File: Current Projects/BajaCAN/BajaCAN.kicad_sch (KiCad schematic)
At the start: 36 parts, among them J1 348300801, J2 348302001, J3 348302004, J4 348300804, SW1 MVIO, U1 MCP1603, U2 MCP251863T-H-SS, U3 AVR128DB32x-xPT, Y1 OV-7604-C7, Y2 CSTNE20M0V530000R0

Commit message: Linked most footprints for Node board
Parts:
- C1, C10, C11, C2, C3, C4, C5, C6, C8, C9: footprint (none) -> Capacitor_SMD:C_0603_1608Metric
- C7: footprint (none) -> Capacitor_SMD:C_Elec_4x5.4
- D1: footprint (none) -> LED_SMD:LED_0805_2012Metric
- L1: footprint (none) -> Inductor_SMD:L_1008_2520Metric
- R1, R2: footprint (none) -> Resistor_SMD:R_0603_1608Metric
- TP1, TP2, TP4: footprint (none) -> TestPoint:TestPoint_Pad_D2.0mm
- TP10, TP5, TP6, TP7, TP8, TP9: footprint (none) -> TestPoint:TestPoint_Pad_D1.0mm
- TP3: footprint (none) -> TestPoint:TestPoint_Pad_D1.5mm
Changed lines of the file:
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@@
 			)
 		)
-		(property "Footprint" ""
+		(property "Footprint" "Capacitor_SMD:C_0603_1608Metric"
 			(at 130.81 41.91 0)
 			(effects
@@
 			)
 		)
-		(property "Footprint" ""
+		(property "Footprint" "TestPoint:TestPoint_Pad_D1.0mm"
 			(at 105.41 71.12 0)
 			(effects
@@
 			)
 		)
-		(property "Footprint" ""
+		(property "Footprint" "TestPoint:TestPoint_Pad_D1.0mm"
 			(at 107.95 73.66 0)
 			(effects
@@
 			)
 		)
-		(property "Footprint" ""
+		(property "Footprint" "TestPoint:TestPoint_Pad_D1.5mm"
 			(at 95.25 49.53 0)
 			(effects
@@
 			)
 		)
-		(property "Footprint" ""
+		(property "Footprint" "Capacitor_SMD:C_0603_1608Metric"
 			(at 146.05 41.91 0)
 			(effects
@@
 			)
 		)
-		(property "Footprint" ""
+		(property "Footprint" "Capacitor_SMD:C_0603_1608Metric"
 			(at 68.58 38.1 0)
 			(effects
@@
 			)
 		)
-		(property "Footprint" ""
+		(property "Footprint" "TestPoint:TestPoint_Pad_D1.0mm"
 			(at 163.83 54.61 0)
 			(effects
@@
 			)
 		)
-		(property "Footprint" ""
+		(property "Footprint" "TestPoint:TestPoint_Pad_D2.0mm"
 			(at 175.26 41.91 0)
 			(effects
@@
 			)
 		)
-		(property "Footprint" ""
+		(property "Footprint" "TestPoint:TestPoint_Pad_D1.0mm"
 			(at 109.22 58.42 0)
 			(effects
@@
 			)
 		)
-		(property "Footprint" ""
+		(property "Footprint" "Capacitor_SMD:C_0603_1608Metric"
 			(at 68.58 41.91 0)
 			(effects
@@
 			)
 		)
-		(property "Footprint" ""
+		(property "Footprint" "Inductor_SMD:L_1008_2520Metric"
 			(at 102.87 22.86 0)
 			(effects
@@
 			)
 		)
-		(property "Footprint" ""
+		(property "Footprint" "Capacitor_SMD:C_Elec_4x5.4"
 			(at 171.45 43.18 0)
 			(effects
@@
 			)
 		)
-		(property "Footprint" ""
+		(property "Footprint" "Capacitor_SMD:C_0603_1608Metric"
 			(at 82.55 49.53 0)
 			(effects
@@
 			)
 		)
-		(property "Footprint" ""
+		(property "Footprint" "Capacitor_SMD:C_0603_1608Metric"
 			(at 105.41 29.21 0)
 			(effects
@@
 			)
 		)
-		(property "Footprint" ""
+		(property "Footprint" "TestPoint:TestPoint_Pad_D2.0mm"
 			(at 107.95 22.86 0)
 			(effects
@@
 			)
 		)
-		(property "Footprint" ""
+		(property "Footprint" "TestPoint:TestPoint_Pad_D2.0mm"
 			(at 175.26 46.99 0)
 			(effects
@@
 			)
 		)
-		(property "Footprint" ""
+		(property "Footprint" "Capacitor_SMD:C_0603_1608Metric"
 			(at 62.23 138.43 0)
 			(effects
@@
 			)
 		)
-		(property "Footprint" ""
+		(property "Footprint" "TestPoint:TestPoint_Pad_D1.0mm"
 			(at 153.67 62.23 0)
 			(effects
@@
 			)
 		)
-		(property "Footprint" ""
+		(property "Footprint" "Resistor_SMD:R_0603_1608Metric"
 			(at 158.75 58.42 0)
 			(effects
@@
 			)
 		)
-		(property "Footprint" ""
+		(property "Footprint" "LED_SMD:LED_0805_2012Metric"
 			(at 33.02 24.13 0)
 			(effects
@@
 			)
 		)
-		(property "Footprint" ""
+		(property "Footprint" "Capacitor_SMD:C_0603_1608Metric"
 			(at 30.48 49.53 0)
 			(effects
@@
 			)
 		)
-		(property "Footprint" ""
+		(property "Footprint" "TestPoint:TestPoint_Pad_D1.0mm"
 			(at 111.76 60.96 0)
 			(effects
@@
 			)
 		)
-		(property "Footprint" ""
+		(property "Footprint" "Capacitor_SMD:C_0603_1608Metric"
 			(at 130.81 45.72 0)
 			(effects
@@
 			)
 		)
-		(property "Footprint" ""
+		(property "Footprint" "Resistor_SMD:R_0603_1608Metric"
 			(at 41.91 25.908 90)
 			(effects
@@
 			)
 		)
-		(property "Footprint" ""
+		(property "Footprint" "Capacitor_SMD:C_0603_1608Metric"
 			(at 78.74 26.67 0)
 			(effects

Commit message: Revert "Merge branch 'main' of github.com:wmBaja/PCB-Design"
This reverts commit fce7a7b580b52db6ba8267641ace841e509f0b35, reversing
changes made to 0a8d1a67a362b0eb6635e51fbc998032cda9d21d.
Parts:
- removed C10: 0.1u, Capacitor_SMD:C_0603_1608Metric, symbol Device:C_Small
- removed D1: POWER, LED_SMD:LED_0805_2012Metric, symbol Device:LED
- removed J1: 348300801, molex:CONN_SD-34829-001_08_ST_MOL, symbol molex:348300801
- removed J4: 348300804, molex:CONN_SD-34829-001_08_ST_MOL, symbol molex:348300801
- removed R1: 1k, Resistor_SMD:R_0603_1608Metric, symbol Device:R
- removed SW1: MVIO, symbol Switch:SW_SPDT
- removed TP1, TP2, TP4: TestPoint, TestPoint:TestPoint_Pad_D2.0mm, symbol Connector:TestPoint
- removed TP10, TP5, TP6, TP7, TP8, TP9: TestPoint, TestPoint:TestPoint_Pad_D1.0mm, symbol Connector:TestPoint
- removed TP3: TestPoint, TestPoint:TestPoint_Pad_D1.5mm, symbol Connector:TestPoint
- added J1: Conn_01x04, symbol Connector_Generic:Conn_01x04
- added J2: ICSP, symbol Connector_Generic:Conn_02x03_Odd_Even
- C1: renamed from C9; footprint Capacitor_SMD:C_0603_1608Metric -> (none)
- C10: renamed from C7; value 10u -> 0.1u; footprint Capacitor_SMD:C_Elec_4x5.4 -> (none)
- C2: renamed from C11; footprint Capacitor_SMD:C_0603_1608Metric -> (none)
- C3, C4, C5: footprint Capacitor_SMD:C_0603_1608Metric -> (none)
- C6: renamed from C8; footprint Capacitor_SMD:C_0603_1608Metric -> (none)
- C7: renamed from C6; footprint Capacitor_SMD:C_0603_1608Metric -> (none)
- C8: renamed from C1; footprint Capacitor_SMD:C_0603_1608Metric -> (none)
- C9: renamed from C2; footprint Capacitor_SMD:C_0603_1608Metric -> (none)
- L1: footprint Inductor_SMD:L_1008_2520Metric -> (none)
- R2: footprint Resistor_SMD:R_0603_1608Metric -> (none)
- Y2: value CSTNE20M0V530000R0 -> CSTNE16M0VH3C000R0
- renumbered D2 to D1, J2 to J3, J3 to J4, U3 to U1, U1 to U3, U2 to U4
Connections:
- net +3.3V: now also U1.10 (VDDIO2)
- net +5V: now also C2.1, J1.1 (Pin_1), J2.2 (Pin_2); no longer C2.2
- net CAN_H: now also J1.3 (Pin_3)
- net CAN_L: now also J1.4 (Pin_4)
- net GND: now also C2.2, J1.2 (Pin_2), J2.6 (Pin_6); no longer C2.1
- net MISO0: now also J2.1 (Pin_1)
- net MOSI0: now also J2.4 (Pin_4)
- net SCK0: now also J2.3 (Pin_3)
- net ~{RESET}: now also J2.5 (Pin_5)
- no-connect marks 9 -> 3
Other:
- note added: "3.3V"
- note removed: "1"
- note removed: "2"
- note removed: "3"
- note removed: "3.3V 5.0V SW1"
- note removed: "4"
- note removed: "5"
- note removed: "5V"
- note removed: "6"
- note removed: "7"
- note removed: "8"
- note removed: "CANH"
- note removed: "CANL"
- note removed: "GND"
- note removed: "MISO"
- note removed: "MOSI"
- note removed: "RESET"
- note removed: "SCK"
- note removed: "X"
- moved on the sheet: C10, C2, C5, C6, C7, C8, C9, D1, L1, R2, U3, U4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

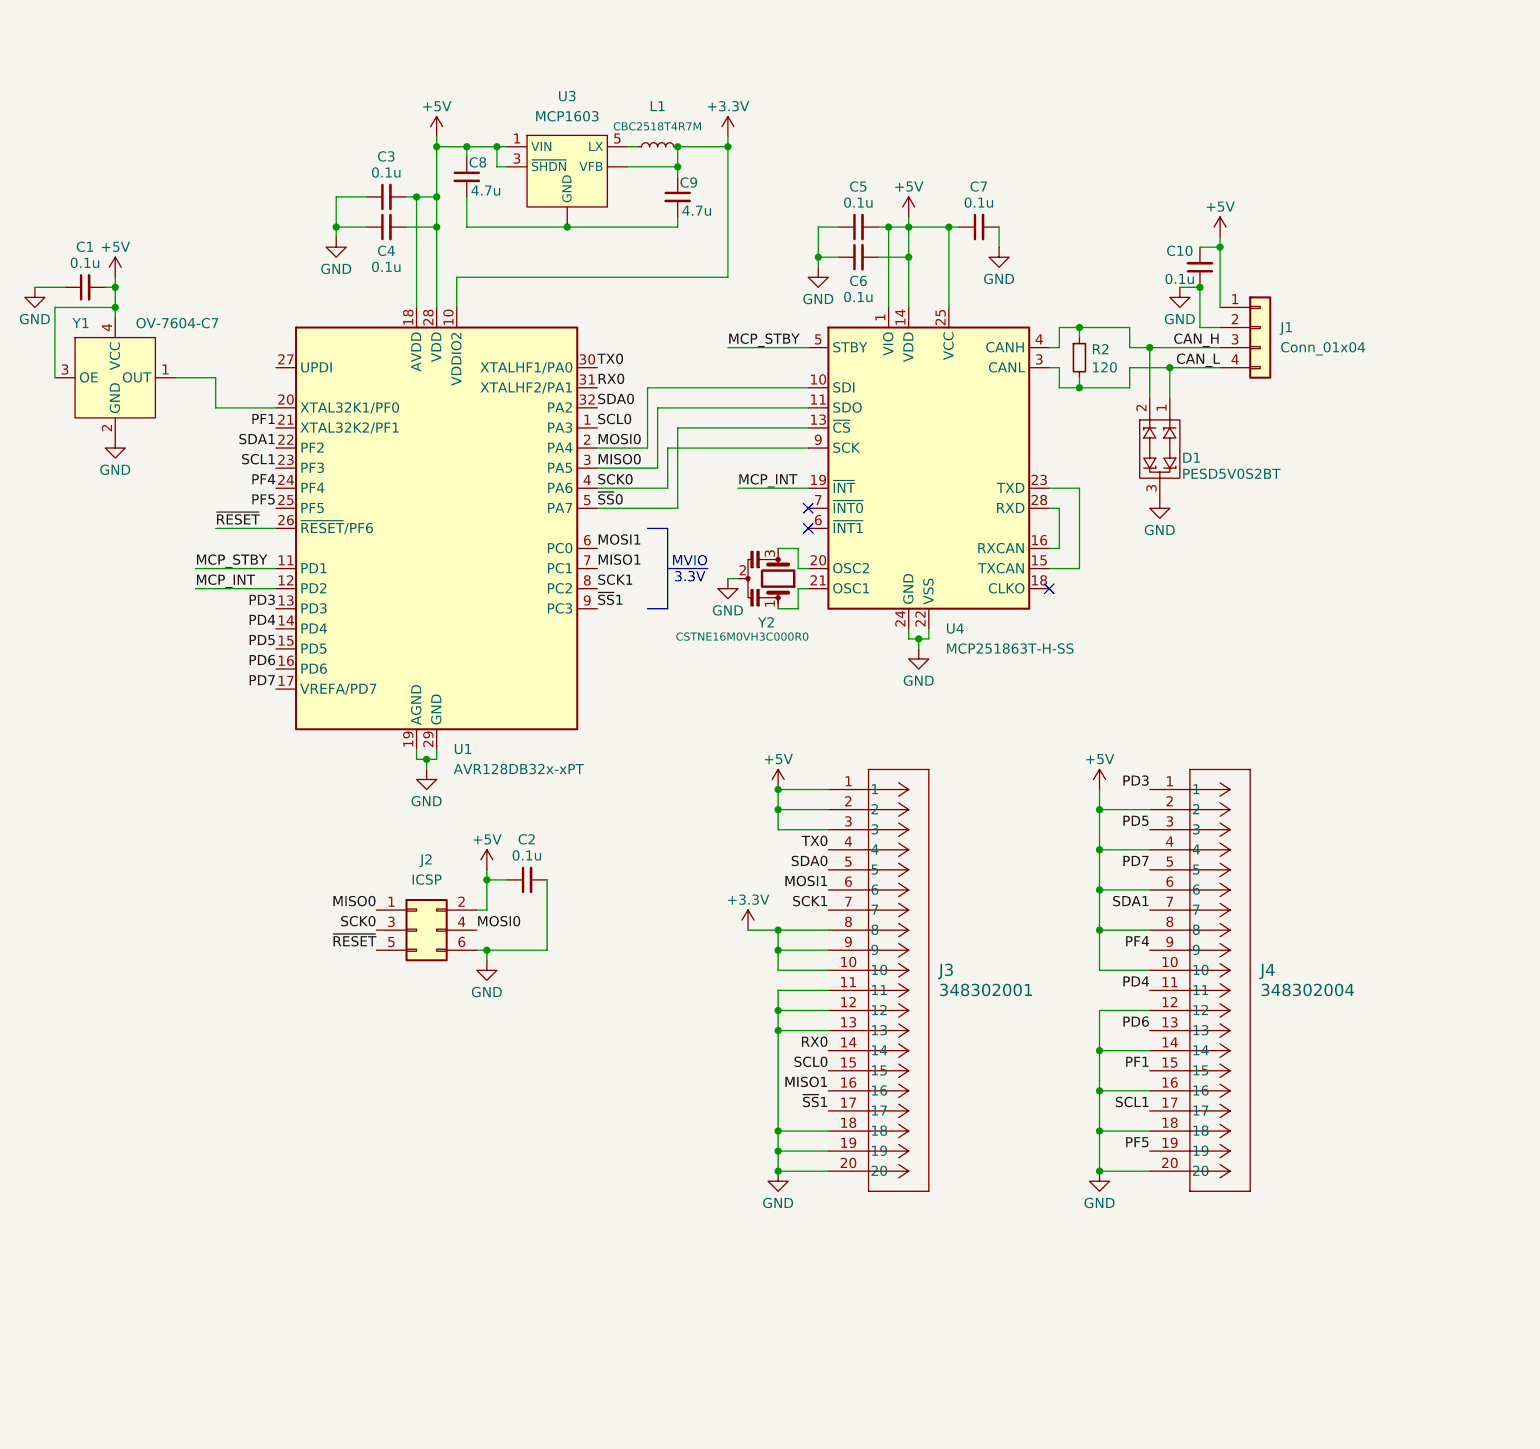
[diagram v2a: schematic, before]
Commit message: CAN Node: Changed CAN clock, added molex 8 pins, MVIO switch, test points
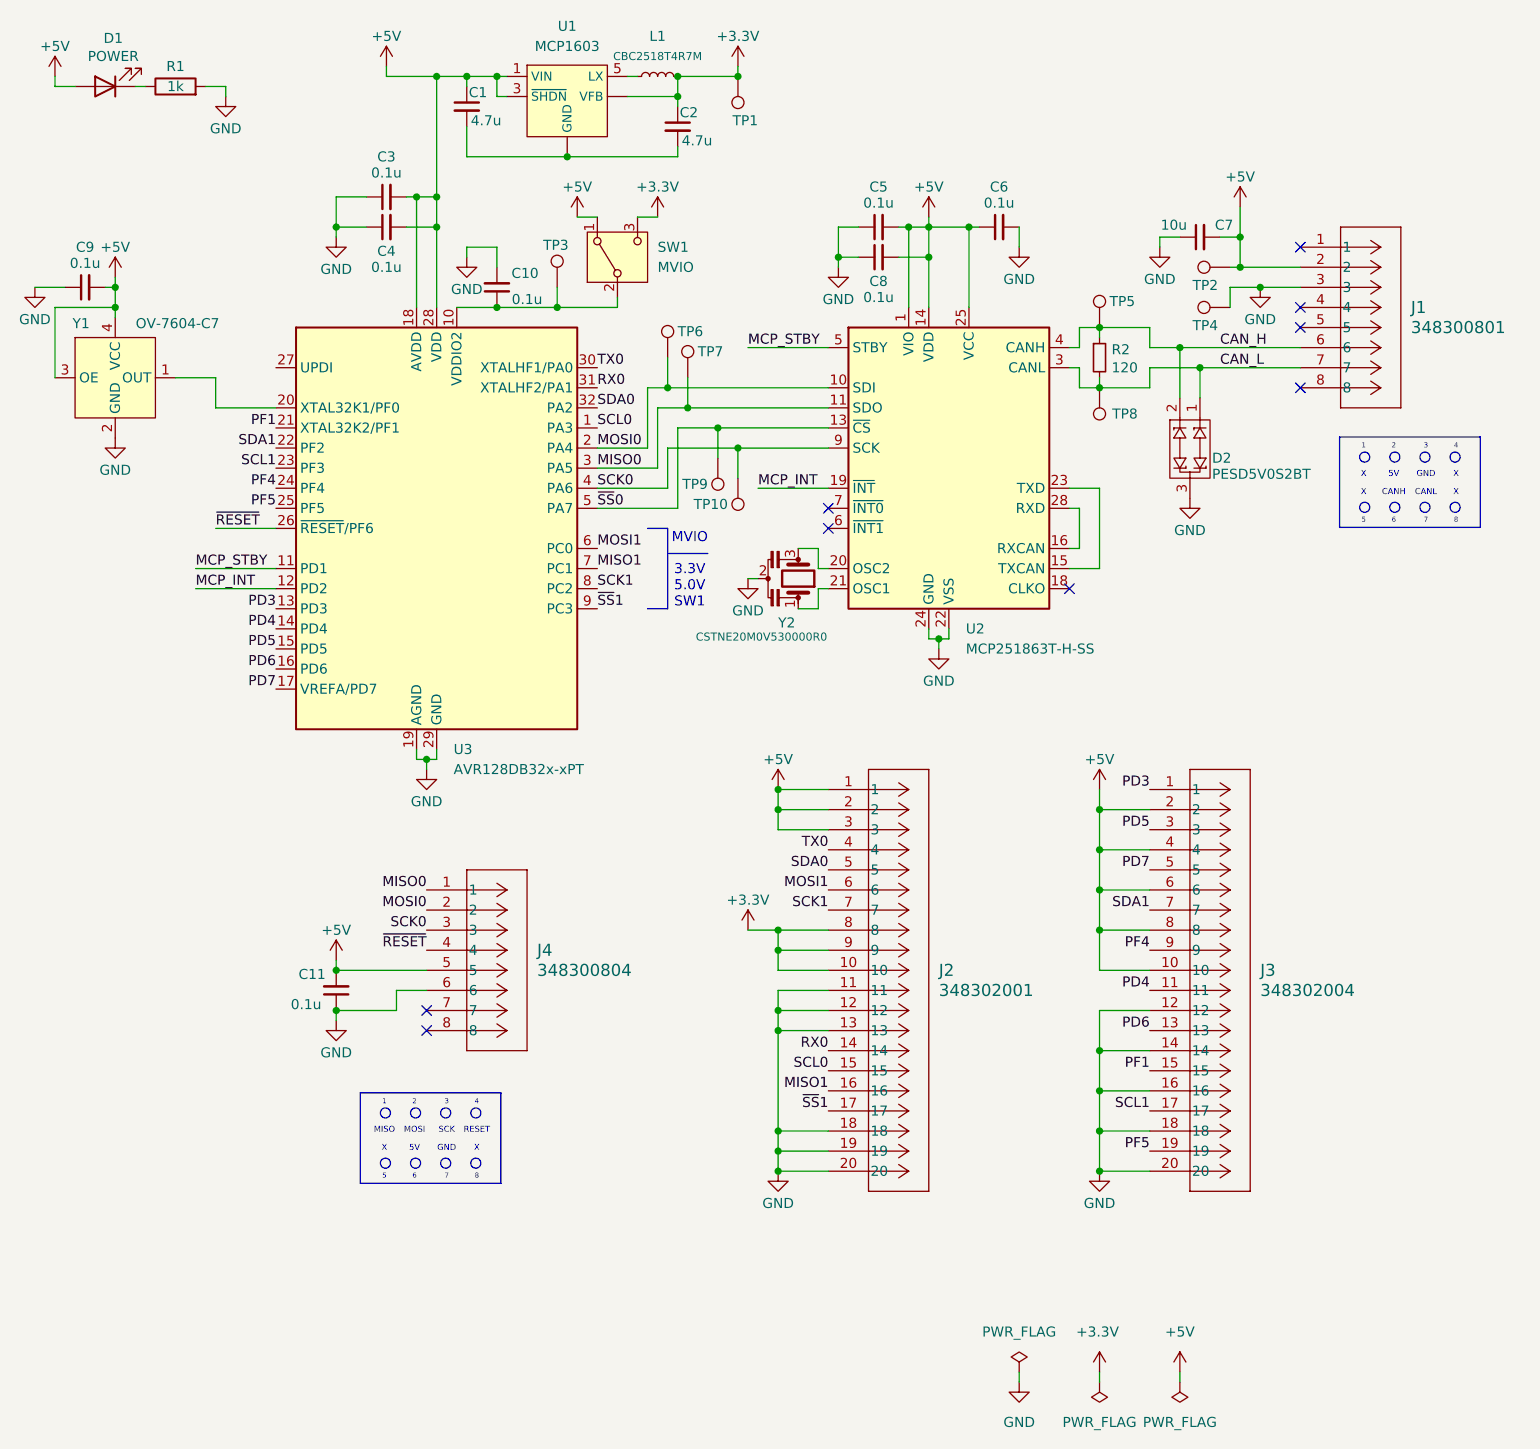
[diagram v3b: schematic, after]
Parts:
- removed J1: Conn_01x04, symbol Connector_Generic:Conn_01x04
- removed J2: ICSP, symbol Connector_Generic:Conn_02x03_Odd_Even
- added C10: 0.1u, symbol Device:C_Small
- added D1: POWER, symbol Device:LED
- added J1: 348300801, molex:CONN_SD-34829-001_08_ST_MOL, symbol molex:348300801
- added J4: 348300804, molex:CONN_SD-34829-001_08_ST_MOL, symbol molex:348300801
- added R1: 1k, symbol Device:R
- added SW1: MVIO, symbol Switch:SW_SPDT
- added TP1, TP10, TP2, TP3, TP4, TP5, TP6, TP7, TP8, TP9: TestPoint, symbol Connector:TestPoint
- C7: renamed from C10; value 0.1u -> 10u
- Y2: value CSTNE16M0VH3C000R0 -> CSTNE20M0V530000R0
- renumbered C8 to C1, C2 to C11, C9 to C2, C7 to C6, C6 to C8, C1 to C9, D1 to D2, J3 to J2, J4 to J3, U3 to U1, U4 to U2, U1 to U3
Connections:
- net +3.3V: now also SW1.3 (C), TP1.1; no longer U3.10 (VDDIO2)
- net +5V: now also C11.2, D1.2 (A), J1.2, J4.5, SW1.1 (A), TP2.1; no longer C11.1
- net CAN_H: now also J1.6, TP5.1
- net CAN_L: now also J1.7, TP8.1
- net GND: now also C11.1, C10.2, J1.3, J4.6, R1.2, TP4.1; no longer C11.2
- net MISO0: now also J4.1, TP7.1
- net MOSI0: now also J4.2, TP6.1
- net SCK0: now also J4.3, TP10.1
- net ~{RESET}: now also J4.4
- net ~{SS}0: now also TP9.1
- new net: C10.1, SW1.2 (B), TP3.1, U3.10 (VDDIO2)
- new net: D1.1 (K), R1.1
- no-connect marks 3 -> 9
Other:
- note added: "1"
- note added: "2"
- note added: "3"
- note added: "3.3V 5.0V SW1"
- note added: "4"
- note added: "5"
- note added: "5V"
- note added: "6"
- note added: "7"
- note added: "8"
- note added: "CANH"
- note added: "CANL"
- note added: "GND"
- note added: "MISO"
- note added: "MOSI"
- note added: "RESET"
- note added: "SCK"
- note added: "X"
- note removed: "3.3V"
- moved on the sheet: C1, C11, C2, C5, C6, C7, C8, D2, L1, R2, U1, U2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
